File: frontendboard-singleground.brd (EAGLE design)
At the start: 158.7 x 58.1 mm, 64 parts, among them U1 MAX2769, X3 BU-SMA-H

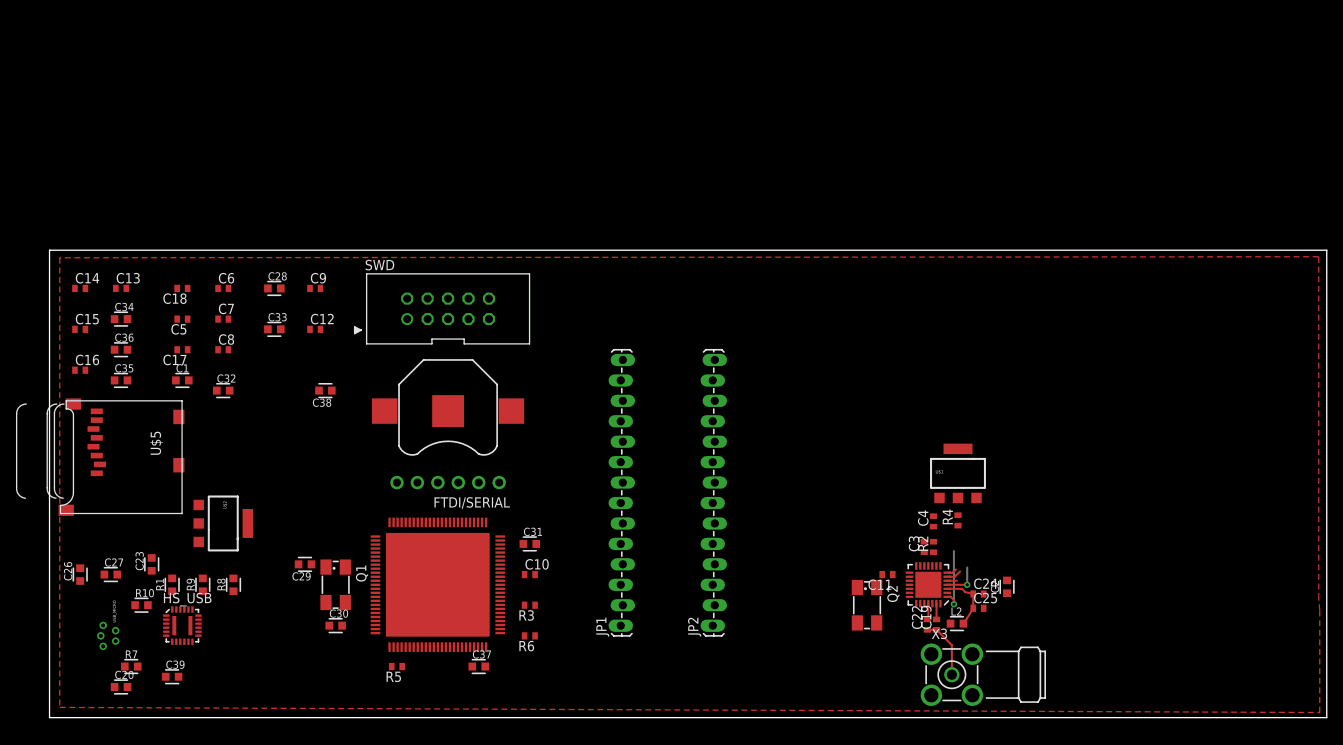
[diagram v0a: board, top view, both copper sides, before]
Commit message: Started board layout with single ground and two power planes on second layer.
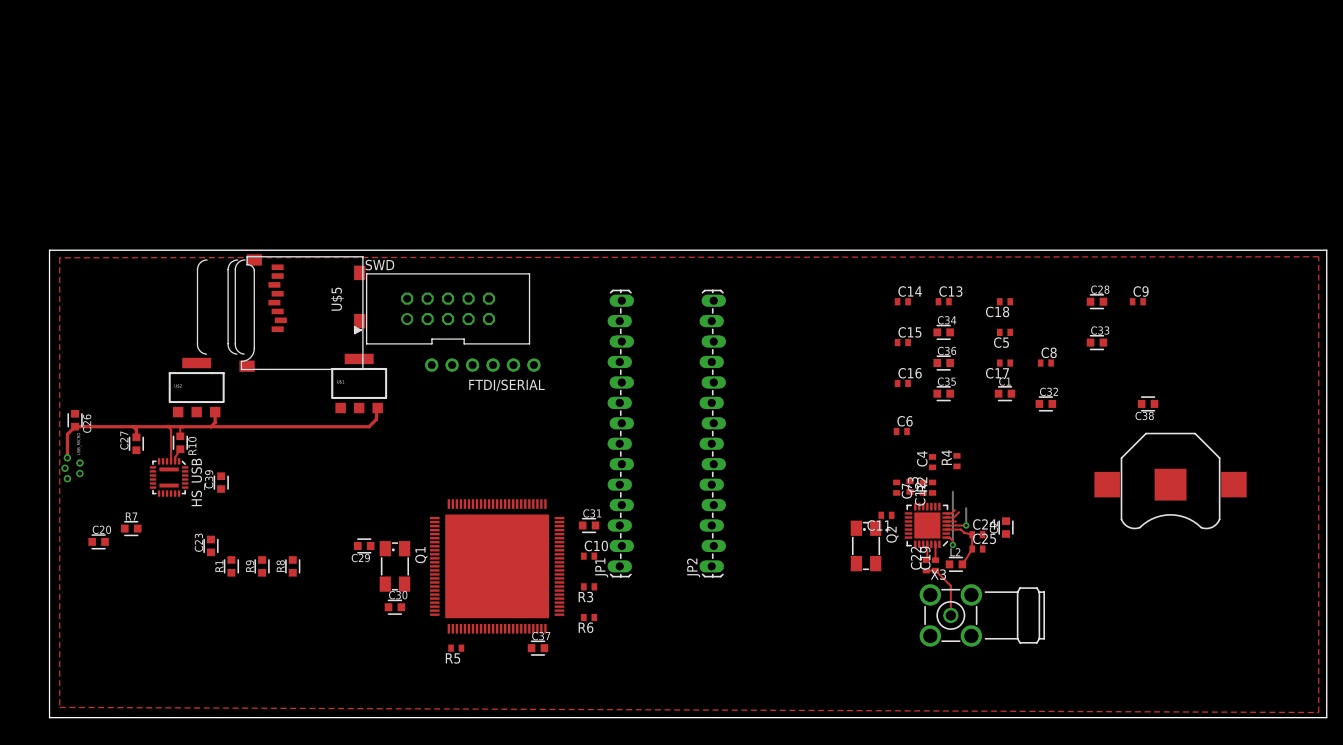
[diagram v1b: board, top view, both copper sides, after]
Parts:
- moved C28 102.2 mm to (130.2, 51.7)
- moved C33 102.2 mm to (130.2, 46.6)
- moved C38 102.2 mm to (136.5, 39.0)
- moved C1 102.2 mm to (118.7, 40.3)
- moved C13 102.2 mm to (111.1, 51.7)
- moved C14 102.2 mm to (106.0, 51.7)
- moved C15 102.2 mm to (106.0, 46.6)
- moved C16 102.2 mm to (106.0, 41.5)
- moved C17 102.2 mm to (118.7, 44.1)
- moved C18 102.2 mm to (118.7, 51.7)
- moved C32 102.2 mm to (123.8, 39.0)
- moved C34 102.2 mm to (111.1, 47.9)
- moved C35 102.2 mm to (111.1, 40.3)
- moved C36 102.2 mm to (111.1, 44.1)
- moved C5 102.2 mm to (118.7, 47.9)
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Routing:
- net 5.0V: track 0.00 -> 53.0 mm
- net VBUS: track 0.00 -> 1.71 mm

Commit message: Change layout for MAX2769 chip. RF header needs pin swap.
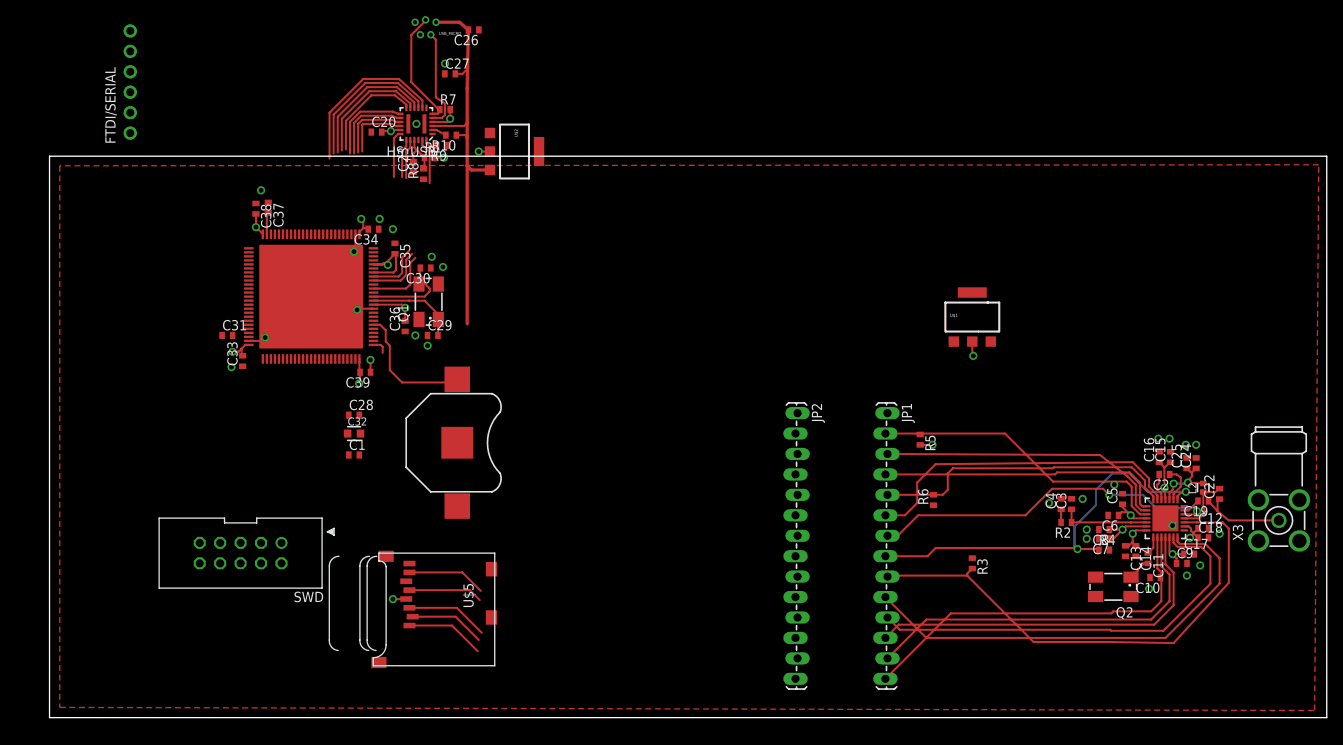
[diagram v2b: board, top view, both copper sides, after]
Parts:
- C1, C2, C20, C23, C26, C27, C28, C29, C30, C31, C33, C34, C35, C36, C37, C38, C39: device rcl_custom:0603-B -> rcl:C0402
- L2: device rcl_custom:0603-B -> rcl_custom:0402-A
- R1, R10, R7, R8, R9: device rcl_custom:0603-B -> rcl:R0402
- moved C38 113.5 mm to (25.7, 63.2), turned to 270 degrees
- moved C33 106.2 mm to (24.0, 44.3), turned to 90 degrees
- moved C28 93.4 mm to (37.8, 37.6)
- moved BAT1 88.8 mm to (50.7, 34.2), turned to 270 degrees
- moved C32 86.1 mm to (37.8, 35.3)
- moved C1 81.3 mm to (37.8, 32.6)
- moved U$1 76.6 mm to (114.7, 49.8)
- moved C34 72.0 mm to (40.3, 60.7), turned to 180 degrees
- moved C35 70.5 mm to (42.9, 58.3), turned to 270 degrees
- moved C10 70.4 mm to (137.4, 17.4), turned to 180 degrees
- moved USB_MICRO 69.8 mm to (46.7, 85.5), turned to 180 degrees
- moved C26 69.3 mm to (52.7, 85.5), turned to 180 degrees
- moved C36 67.1 mm to (44.2, 48.6), turned to 90 degrees
- moved R7 65.0 mm to (49.1, 75.6)
- moved C37 64.2 mm to (27.2, 63.4), turned to 270 degrees
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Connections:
- net 3.3VD: no longer U$3.P$22
- net BAR_GND: no longer U$3.P$20
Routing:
- net IDLE: track 0.00 -> 62.9 mm
- net I1: track 0.00 -> 56.2 mm
- net I0: track 0.00 -> 52.6 mm
- net CLKOUT: track 0.00 -> 46.6 mm
- net Q0: track 0.00 -> 46.4 mm
- net Q1: track 0.00 -> 46.4 mm
- net 3.3VD: track 0.00 -> 45.0 mm, vias 0 -> 13
- net PGM: track 0.00 -> 43.8 mm, vias 0 -> 2
- net ANTFLAG: track 8.11 -> 50.3 mm, vias 1 -> 2
- net LD: track 1.87 -> 40.8 mm
- net SPI_CS: track 0.00 -> 38.5 mm
- net SHDN: track 1.26 -> 38.1 mm
- net SPI_CLK: track 0.00 -> 36.3 mm
- net SPI_MOSI: track 0.00 -> 35.9 mm
- net 3.3VA: track 4.64 -> 28.4 mm, vias 1 -> 6
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- added copper zone on layer 2, net 3.3VD
- added copper zone on layer 3, net BAR_GND
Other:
- board size 158.7 x 58.1 mm -> 158.7 x 69.8 mm

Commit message: RF side signals routed except for power.
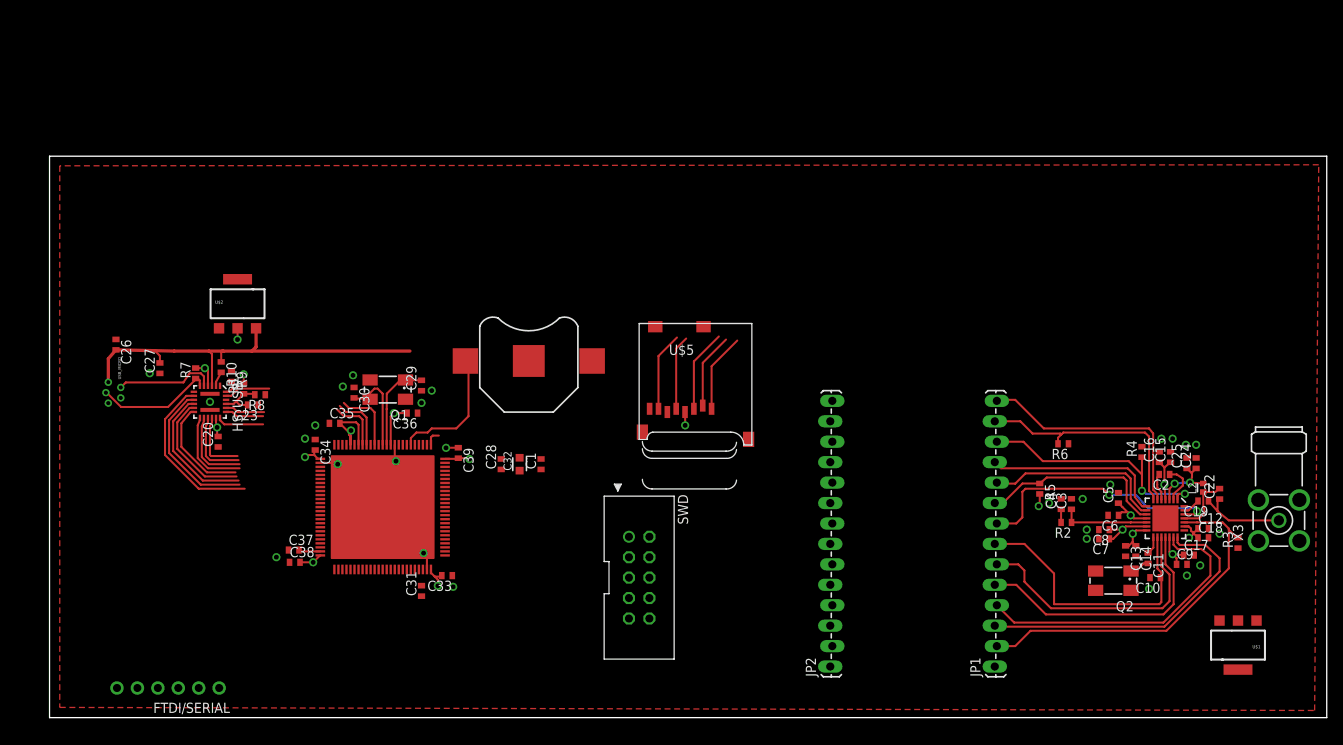
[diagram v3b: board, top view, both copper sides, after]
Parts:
- moved FTDI/SERIAL 75.5 mm to (14.7, 3.68), turned to 180 degrees
- moved USB_MICRO 59.3 mm to (8.26, 40.4), turned to 270 degrees
- moved C26 59.2 mm to (8.26, 46.4), turned to 270 degrees
- moved U$1 52.5 mm to (147.7, 9.02), turned to 180 degrees
- moved C27 51.4 mm to (13.7, 43.4), turned to 90 degrees
- moved SWD 49.6 mm to (73.3, 17.4), turned to 270 degrees
- moved R7 45.1 mm to (18.2, 42.8), turned to 90 degrees
- moved C38 44.2 mm to (30.5, 19.3), turned to 0 degrees
- moved C20 43.2 mm to (21.0, 34.3), turned to 90 degrees
- moved HS_USB 43.0 mm to (19.9, 39.2), turned to 270 degrees
- moved C37 42.7 mm to (30.4, 20.8), turned to 0 degrees
- moved R10 40.6 mm to (21.3, 43.6), turned to 270 degrees
- moved C31 39.9 mm to (46.2, 15.7), turned to 90 degrees
- moved U$2 39.3 mm to (23.4, 51.4), turned to 0 degrees
- moved R9 38.8 mm to (22.6, 42.4), turned to 270 degrees
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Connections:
- net ANTFLAG: now also JP1.12, JP2.12, U$3.P$61; no longer JP1.8, JP2.8, U$3.P$57
- net CLKOUT: now also JP1.7, JP2.7, U$3.P$56; no longer JP1.14, JP2.14, U$3.P$63
- net I0: now also JP1.4, JP2.4, U$3.P$32; no longer JP1.11, JP2.11, U$3.P$60
- net I1: now also JP1.3, JP2.3, U$3.P$89; no longer JP1.10, JP2.10, U$3.P$59
- net IDLE: now also JP1.2, JP2.2, U$3.P$29; no longer JP1.9, JP2.9, U$3.P$58
- net LD: now also JP1.14, JP2.14, U$3.P$63; no longer JP1.6, JP2.6, U$3.P$55
- net PGM: now also JP1.8, JP2.8, U$3.P$57; no longer JP1.7, JP2.7, U$3.P$56
- net Q0: now also JP1.5, JP2.5, U$3.P$54; no longer JP1.12, JP2.12, U$3.P$61
- net Q1: now also JP1.6, JP2.6, U$3.P$55; no longer JP1.13, JP2.13, U$3.P$62
- net SHDN: now also JP1.13, JP2.13, U$3.P$62; no longer JP1.5, JP2.5, U$3.P$54
- net SPI_CLK: now also JP1.10, JP2.10, U$3.P$59; no longer JP1.3, JP2.3, U$3.P$89
- net SPI_CS: now also JP1.9, JP2.9, U$3.P$58; no longer JP1.2, JP2.2, U$3.P$29
- net SPI_MOSI: now also JP1.11, JP2.11, U$3.P$60; no longer JP1.4, JP2.4, U$3.P$32
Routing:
- net ANTFLAG: track 50.3 -> 30.9 mm
- net IDLE: track 62.9 -> 45.2 mm
- net I1: track 56.2 -> 39.2 mm
- net SPI_CS: track 38.5 -> 23.5 mm
- net I0: track 52.6 -> 38.3 mm
- net SPI_CLK: track 36.3 -> 22.6 mm
- net Q0: track 46.4 -> 33.0 mm
- net Q1: track 46.4 -> 33.3 mm
- net SPI_MOSI: track 35.9 -> 22.8 mm
- net PGM: track 43.8 -> 31.5 mm
- net CLKOUT: track 46.6 -> 34.6 mm
- net LD: track 40.8 -> 29.7 mm
- net SHDN: track 38.1 -> 29.5 mm
- net 3.3VA: track 28.4 -> 27.1 mm, vias 6 -> 5
- net BAR_GND: vias 28 -> 27

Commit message: Fixed reversed P26,P28 reversed on STM32F4. Better layout on digital side. Incomplete.
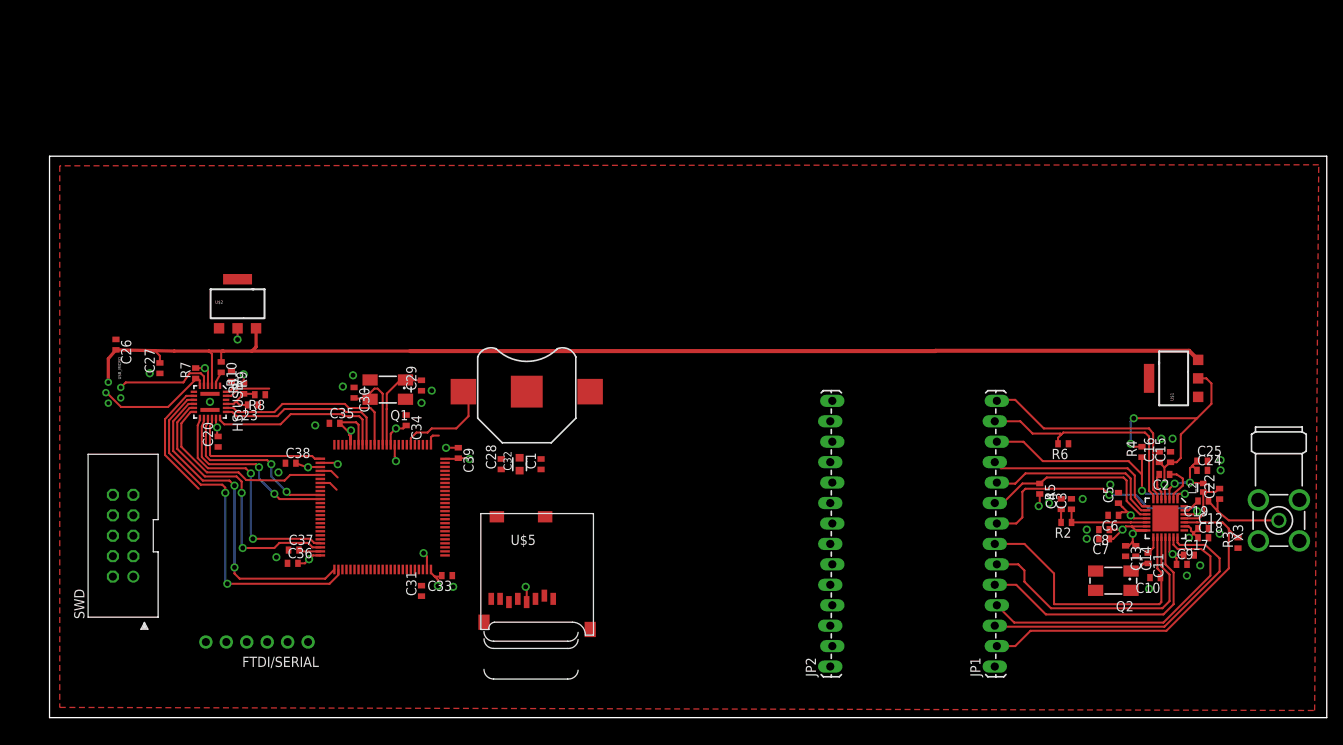
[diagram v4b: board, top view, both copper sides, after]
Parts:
- moved SWD 64.3 mm to (9.14, 22.6), turned to 90 degrees
- moved U$1 34.1 mm to (139.7, 42.2), turned to 90 degrees
- moved U$5 30.7 mm to (53.6, 25.4)
- moved C36 23.9 mm to (30.2, 19.2), turned to 0 degrees
- moved FTDI/SERIAL 12.4 mm to (25.8, 9.40)
- moved C38 12.3 mm to (30.0, 31.6)
- moved C34 11.7 mm to (44.3, 37.0)
- moved BAT1 3.82 mm to (59.3, 40.5)
- moved C25 1.92 mm to (143.3, 31.9), turned to 0 degrees
- moved C24 1.17 mm to (143.3, 30.7), turned to 0 degrees
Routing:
- net 5.0V: track 51.8 -> 150.2 mm
- net 3.3VA: track 27.1 -> 56.1 mm, vias 5 -> 7
- net OTG_HS_ULPI_D6: track 18.7 -> 44.0 mm, vias 0 -> 2
- net OTG_HS_ULPI_D5: track 16.9 -> 40.7 mm, vias 0 -> 2
- net OTG_HS_ULPI_D4: track 15.0 -> 34.3 mm, vias 0 -> 2
- net OTG_HS_ULPI_D3: track 10.8 -> 29.2 mm, vias 0 -> 2
- net OTG_HS_ULPI_D1: track 9.07 -> 21.9 mm, vias 0 -> 2
- net OTG_HS_ULPI_D2: track 9.98 -> 22.6 mm, vias 0 -> 2
- net OTG_HS_ULPI_CLK: track 13.2 -> 24.4 mm
- net OTG_HS_ULPI_D0: track 8.14 -> 18.6 mm
- net SDIO_CMD: track 10.3 -> 0.00 mm
- net OTG_HS_ULPI_STP: track 13.3 -> 23.6 mm
- net SDIO_D0: track 9.81 -> 0.00 mm
- net SDIO_D2: track 9.80 -> 0.00 mm
- net OTG_HS_ULPI_DIR: track 12.1 -> 21.9 mm
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
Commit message: Layout done and verified. Fails Laen's DRU for layer setup issues.
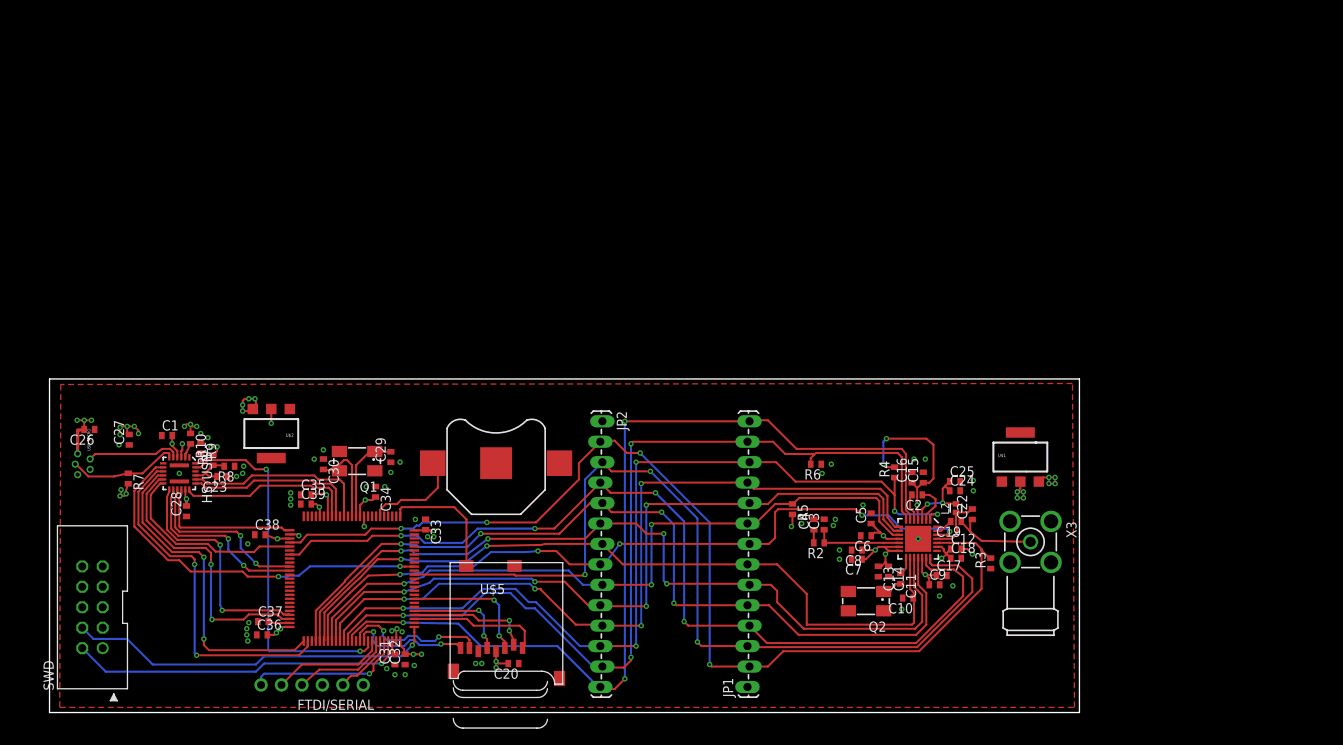
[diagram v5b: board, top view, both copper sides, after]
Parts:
- C32: device rcl_custom:0603-B -> rcl:C0402
- moved C1 46.6 mm to (14.6, 35.1), turned to 0 degrees
- moved C20 45.9 mm to (57.7, 6.73), turned to 180 degrees
- moved JP2 41.8 mm to (68.6, 36.8), turned to 270 degrees
- moved C28 39.5 mm to (17.0, 25.7)
- moved X3 31.0 mm to (121.9, 21.8), turned to 270 degrees
- moved C11 30.8 mm to (105.8, 17.3)
- moved C12 30.8 mm to (112.6, 21.0)
- moved C14 30.8 mm to (104.3, 18.2)
- moved C18 30.8 mm to (112.6, 19.8)
- moved C19 30.8 mm to (112.6, 24.4)
- moved C4 30.8 mm to (95.0, 24.0)
- moved C5 30.8 mm to (102.1, 24.8)
- moved C9 30.8 mm to (110.0, 16.5)
- moved JP1 30.8 mm to (86.9, 3.81)
- moved L2 30.8 mm to (112.6, 26.0)
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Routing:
- net 5.0V: track 150.2 -> 27.0 mm, vias 0 -> 20
- net LD: track 29.7 -> 116.4 mm, vias 0 -> 3
- net SHDN: track 29.5 -> 113.6 mm, vias 0 -> 3
- net IDLE: track 47.7 -> 130.8 mm, vias 0 -> 4
- net ANTFLAG: track 30.9 -> 110.5 mm, vias 2 -> 5
- net SPI_MOSI: track 22.8 -> 97.6 mm, vias 0 -> 4
- net Q0: track 33.0 -> 107.3 mm, vias 0 -> 4
- net I0: track 40.7 -> 114.6 mm, vias 0 -> 4
- net I1: track 39.2 -> 111.8 mm, vias 0 -> 3
- net SPI_CLK: track 22.6 -> 92.6 mm, vias 0 -> 4
- net Q1: track 33.3 -> 102.1 mm, vias 0 -> 4
- net SPI_CS: track 23.5 -> 88.6 mm, vias 0 -> 3
- net CLKOUT: track 34.6 -> 95.3 mm, vias 0 -> 2
- net PGM: track 31.5 -> 92.1 mm, vias 2 -> 5
- net SWCLK: track 0.00 -> 46.2 mm, vias 0 -> 1
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- added copper zone on layer 3, net 3.3VA
- added copper zone on layer 3, net 3.3VD
- added copper zone on layer 3, net 5.0V
- added copper zone on layer 2, net BAR_GND
- removed copper zone on layer 2, net 3.3VD
- removed copper zone on layer 3, net BAR_GND
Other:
- board size 158.7 x 69.8 mm -> 128 x 41.5 mm
